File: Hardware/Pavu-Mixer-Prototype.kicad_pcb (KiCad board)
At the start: 2 copper layers, 155.9 x 91.9 mm, 11 parts, among them SW1 SW_MEC_5G_2LED, SW2 SW_MEC_5G_2LED, SW3 SW_MEC_5G_2LED, SW4 SW_MEC_5G_2LED, SW5 SW_MEC_5G_2LED

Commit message: Mounting Holes
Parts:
- added H1: MountingHole_Pad, MountingHole:MountingHole_3.5mm_Pad_Via, F.Cu at (30.4, 29.9)
- added H2: MountingHole_Pad, MountingHole:MountingHole_3.5mm_Pad_Via, F.Cu at (30.4, 112.0)
- added H3: MountingHole_Pad, MountingHole:MountingHole_3.5mm_Pad_Via, F.Cu at (175.4, 29.9)
- added H4: MountingHole_Pad, MountingHole:MountingHole_3.5mm_Pad_Via, F.Cu at (175.4, 112.0)
- moved D1 2.50 mm to (143.8, 42.5)
- moved SW1 2.50 mm to (77.5, 86.7)
- moved SW2 2.50 mm to (77.5, 105.0)
- moved SW3 2.50 mm to (92.5, 86.7)
- moved SW4 2.50 mm to (92.5, 105.0)
- moved SW5 2.50 mm to (147.5, 102.5)
- moved VOL_CH1 2.50 mm to (37.5, 42.5)
- moved VOL_CH2 2.50 mm to (52.5, 42.5)
- moved VOL_CH3 2.50 mm to (110.0, 42.5)
- moved VOL_CH4 2.50 mm to (125.0, 42.5)
- moved VOL_MASTER1 2.50 mm to (162.5, 42.5)

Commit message: GND Net for mounting holes
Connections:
- H1 pad 1: Net-(H1-Pad1) -> GND
- H2 pad 1: Net-(H2-Pad1) -> GND
- H3 pad 1: Net-(H3-Pad1) -> GND
- H4 pad 1: Net-(H4-Pad1) -> GND
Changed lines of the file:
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@@
     (zones 0)
     (modules 15)
-    (nets 5)
+    (nets 2)
   )
   (page A4)
@@
   )
   (net 0 "")
-  (net 1 "Net-(H1-Pad1)")
-  (net 2 "Net-(H2-Pad1)")
-  (net 3 "Net-(H3-Pad1)")
-  (net 4 "Net-(H4-Pad1)")
+  (net 1 GND)
   (net_class Default "This is the default net class."
     (clearance 0.2)
@@
     (uvia_dia 0.3)
     (uvia_drill 0.1)
+    (add_net GND)
     (add_net "Net-(D1-Pad1)")
     (add_net "Net-(D1-Pad10)")
@@
     (add_net "Net-(D1-Pad8)")
     (add_net "Net-(D1-Pad9)")
-    (add_net "Net-(H1-Pad1)")
-    (add_net "Net-(H2-Pad1)")
-    (add_net "Net-(H3-Pad1)")
-    (add_net "Net-(H4-Pad1)")
     (add_net "Net-(SW1-Pad1)")
     (add_net "Net-(SW1-Pad2)")
@@
     (fp_circle (center 0 0) (end 3.75 0) (layer F.CrtYd) (width 0.05))
     (pad 1 thru_hole circle (at 1.856155 -1.856155) (size 0.8 0.8) (drill 0.5) (layers *.Cu *.Mask)
-      (net 4 "Net-(H4-Pad1)"))
+      (net 1 GND))
     (pad 1 thru_hole circle (at 0 -2.625) (size 0.8 0.8) (drill 0.5) (layers *.Cu *.Mask)
-      (net 4 "Net-(H4-Pad1)"))
+      (net 1 GND))
     (pad 1 thru_hole circle (at -1.856155 -1.856155) (size 0.8 0.8) (drill 0.5) (layers *.Cu *.Mask)
-      (net 4 "Net-(H4-Pad1)"))
+      (net 1 GND))
     (pad 1 thru_hole circle (at -2.625 0) (size 0.8 0.8) (drill 0.5) (layers *.Cu *.Mask)
-      (net 4 "Net-(H4-Pad1)"))
+      (net 1 GND))
     (pad 1 thru_hole circle (at -1.856155 1.856155) (size 0.8 0.8) (drill 0.5) (layers *.Cu *.Mask)
-      (net 4 "Net-(H4-Pad1)"))
+      (net 1 GND))
     (pad 1 thru_hole circle (at 0 2.625) (size 0.8 0.8) (drill 0.5) (layers *.Cu *.Mask)
-      (net 4 "Net-(H4-Pad1)"))
+      (net 1 GND))
     (pad 1 thru_hole circle (at 1.856155 1.856155) (size 0.8 0.8) (drill 0.5) (layers *.Cu *.Mask)
-      (net 4 "Net-(H4-Pad1)"))
+      (net 1 GND))
     (pad 1 thru_hole circle (at 2.625 0) (size 0.8 0.8) (drill 0.5) (layers *.Cu *.Mask)
-      (net 4 "Net-(H4-Pad1)"))
+      (net 1 GND))
     (pad 1 thru_hole circle (at 0 0) (size 7 7) (drill 3.5) (layers *.Cu *.Mask)
-      (net 4 "Net-(H4-Pad1)"))
+      (net 1 GND))
   )
   (module MountingHole:MountingHole_3.5mm_Pad_Via (layer F.Cu)
@@
     (fp_circle (center 0 0) (end 3.75 0) (layer F.CrtYd) (width 0.05))
     (pad 1 thru_hole circle (at 1.856155 -1.856155) (size 0.8 0.8) (drill 0.5) (layers *.Cu *.Mask)
-      (net 3 "Net-(H3-Pad1)"))
+      (net 1 GND))
     (pad 1 thru_hole circle (at 0 -2.625) (size 0.8 0.8) (drill 0.5) (layers *.Cu *.Mask)
-      (net 3 "Net-(H3-Pad1)"))
+      (net 1 GND))
     (pad 1 thru_hole circle (at -1.856155 -1.856155) (size 0.8 0.8) (drill 0.5) (layers *.Cu *.Mask)
-      (net 3 "Net-(H3-Pad1)"))
+      (net 1 GND))
     (pad 1 thru_hole circle (at -2.625 0) (size 0.8 0.8) (drill 0.5) (layers *.Cu *.Mask)
-      (net 3 "Net-(H3-Pad1)"))
+      (net 1 GND))
     (pad 1 thru_hole circle (at -1.856155 1.856155) (size 0.8 0.8) (drill 0.5) (layers *.Cu *.Mask)
-      (net 3 "Net-(H3-Pad1)"))
+      (net 1 GND))
     (pad 1 thru_hole circle (at 0 2.625) (size 0.8 0.8) (drill 0.5) (layers *.Cu *.Mask)
-      (net 3 "Net-(H3-Pad1)"))
+      (net 1 GND))
     (pad 1 thru_hole circle (at 1.856155 1.856155) (size 0.8 0.8) (drill 0.5) (layers *.Cu *.Mask)
-      (net 3 "Net-(H3-Pad1)"))
+      (net 1 GND))
     (pad 1 thru_hole circle (at 2.625 0) (size 0.8 0.8) (drill 0.5) (layers *.Cu *.Mask)
-      (net 3 "Net-(H3-Pad1)"))
+      (net 1 GND))
     (pad 1 thru_hole circle (at 0 0) (size 7 7) (drill 3.5) (layers *.Cu *.Mask)
-      (net 3 "Net-(H3-Pad1)"))
+      (net 1 GND))
   )
   (module MountingHole:MountingHole_3.5mm_Pad_Via (layer F.Cu)
@@
     (fp_circle (center 0 0) (end 3.75 0) (layer F.CrtYd) (width 0.05))
     (pad 1 thru_hole circle (at 1.856155 -1.856155) (size 0.8 0.8) (drill 0.5) (layers *.Cu *.Mask)
-      (net 2 "Net-(H2-Pad1)"))
+      (net 1 GND))
     (pad 1 thru_hole circle (at 0 -2.625) (size 0.8 0.8) (drill 0.5) (layers *.Cu *.Mask)
-      (net 2 "Net-(H2-Pad1)"))
+      (net 1 GND))
     (pad 1 thru_hole circle (at -1.856155 -1.856155) (size 0.8 0.8) (drill 0.5) (layers *.Cu *.Mask)
-      (net 2 "Net-(H2-Pad1)"))
+      (net 1 GND))
     (pad 1 thru_hole circle (at -2.625 0) (size 0.8 0.8) (drill 0.5) (layers *.Cu *.Mask)
-      (net 2 "Net-(H2-Pad1)"))
+      (net 1 GND))
     (pad 1 thru_hole circle (at -1.856155 1.856155) (size 0.8 0.8) (drill 0.5) (layers *.Cu *.Mask)
-      (net 2 "Net-(H2-Pad1)"))
+      (net 1 GND))
     (pad 1 thru_hole circle (at 0 2.625) (size 0.8 0.8) (drill 0.5) (layers *.Cu *.Mask)
-      (net 2 "Net-(H2-Pad1)"))
+      (net 1 GND))
     (pad 1 thru_hole circle (at 1.856155 1.856155) (size 0.8 0.8) (drill 0.5) (layers *.Cu *.Mask)
-      (net 2 "Net-(H2-Pad1)"))
+      (net 1 GND))
     (pad 1 thru_hole circle (at 2.625 0) (size 0.8 0.8) (drill 0.5) (layers *.Cu *.Mask)
-      (net 2 "Net-(H2-Pad1)"))
+      (net 1 GND))
     (pad 1 thru_hole circle (at 0 0) (size 7 7) (drill 3.5) (layers *.Cu *.Mask)
-      (net 2 "Net-(H2-Pad1)"))
+      (net 1 GND))
   )
   (module MountingHole:MountingHole_3.5mm_Pad_Via (layer F.Cu)
@@
     (fp_circle (center 0 0) (end 3.75 0) (layer F.CrtYd) (width 0.05))
     (pad 1 thru_hole circle (at 1.856155 -1.856155) (size 0.8 0.8) (drill 0.5) (layers *.Cu *.Mask)
-      (net 1 "Net-(H1-Pad1)"))
+      (net 1 GND))
     (pad 1 thru_hole circle (at 0 -2.625) (size 0.8 0.8) (drill 0.5) (layers *.Cu *.Mask)
-      (net 1 "Net-(H1-Pad1)"))
+      (net 1 GND))
     (pad 1 thru_hole circle (at -1.856155 -1.856155) (size 0.8 0.8) (drill 0.5) (layers *.Cu *.Mask)
-      (net 1 "Net-(H1-Pad1)"))
+      (net 1 GND))
     (pad 1 thru_hole circle (at -2.625 0) (size 0.8 0.8) (drill 0.5) (layers *.Cu *.Mask)
-      (net 1 "Net-(H1-Pad1)"))
+      (net 1 GND))
     (pad 1 thru_hole circle (at -1.856155 1.856155) (size 0.8 0.8) (drill 0.5) (layers *.Cu *.Mask)
-      (net 1 "Net-(H1-Pad1)"))
+      (net 1 GND))
     (pad 1 thru_hole circle (at 0 2.625) (size 0.8 0.8) (drill 0.5) (layers *.Cu *.Mask)
-      (net 1 "Net-(H1-Pad1)"))
+      (net 1 GND))
     (pad 1 thru_hole circle (at 1.856155 1.856155) (size 0.8 0.8) (drill 0.5) (layers *.Cu *.Mask)
-      (net 1 "Net-(H1-Pad1)"))
+      (net 1 GND))
     (pad 1 thru_hole circle (at 2.625 0) (size 0.8 0.8) (drill 0.5) (layers *.Cu *.Mask)
-      (net 1 "Net-(H1-Pad1)"))
+      (net 1 GND))
     (pad 1 thru_hole circle (at 0 0) (size 7 7) (drill 3.5) (layers *.Cu *.Mask)
-      (net 1 "Net-(H1-Pad1)"))
+      (net 1 GND))
   )
   (module Pavu-Mixer-Prototype:Potentiometer_Alps_RS60_Double_Slide (layer F.Cu)

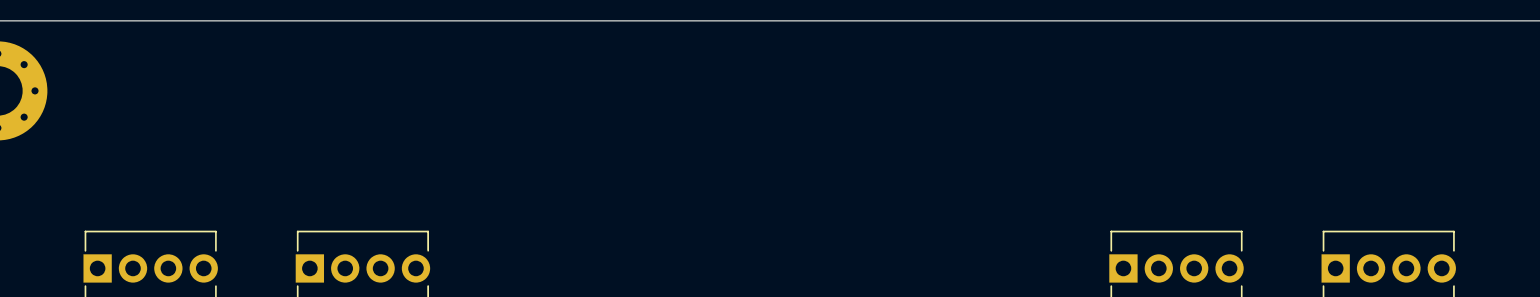
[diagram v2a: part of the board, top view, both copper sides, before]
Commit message: Add channel LEDs
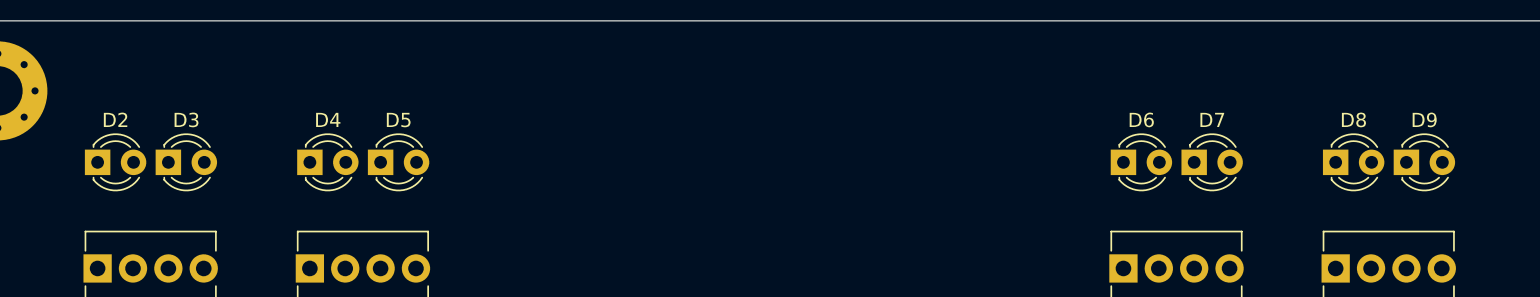
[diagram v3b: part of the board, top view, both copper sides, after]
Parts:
- added D2: LED, LED_THT:LED_D3.0mm, F.Cu at (37.5, 35.0)
- added D3: LED, LED_THT:LED_D3.0mm_Clear, F.Cu at (42.5, 35.0)
- added D4: LED, LED_THT:LED_D3.0mm, F.Cu at (52.5, 35.0)
- added D5: LED, LED_THT:LED_D3.0mm_Clear, F.Cu at (57.5, 35.0)
- added D6: LED, LED_THT:LED_D3.0mm, F.Cu at (110.0, 35.0)
- added D7: LED, LED_THT:LED_D3.0mm_Clear, F.Cu at (115.0, 35.0)
- added D8: LED, LED_THT:LED_D3.0mm, F.Cu at (125.0, 35.0)
- added D9: LED, LED_THT:LED_D3.0mm_Clear, F.Cu at (130.0, 35.0)

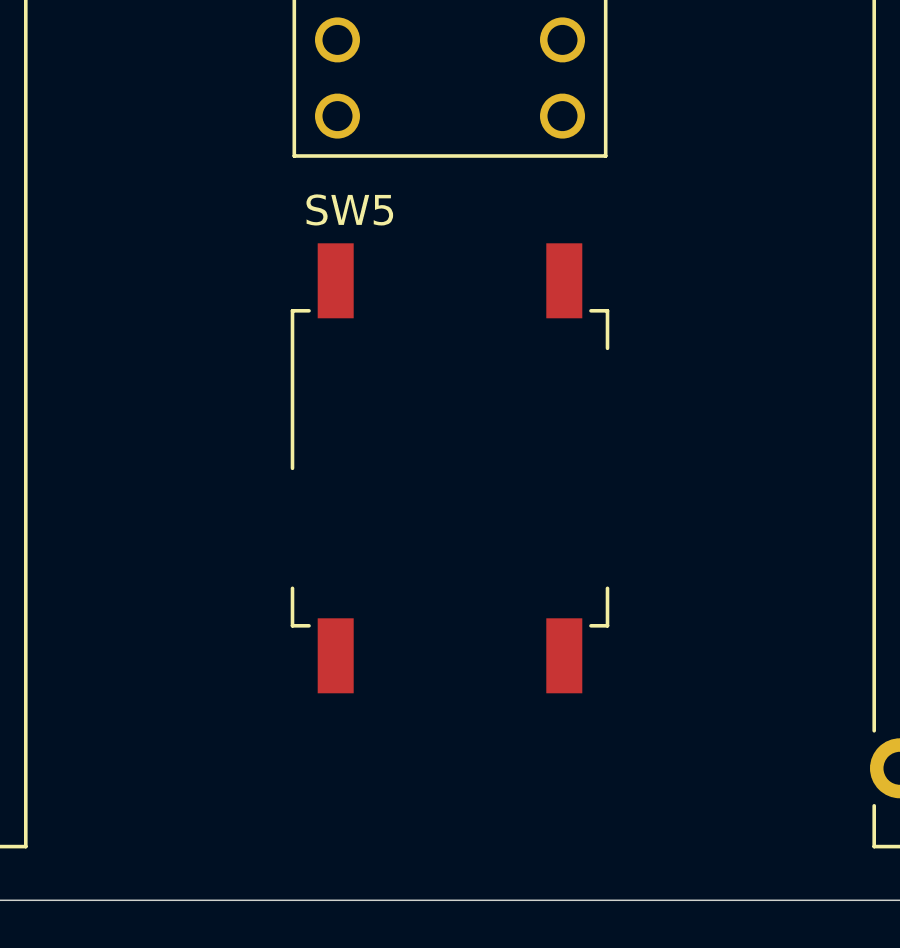
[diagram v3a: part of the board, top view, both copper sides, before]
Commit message: Fix master mute position
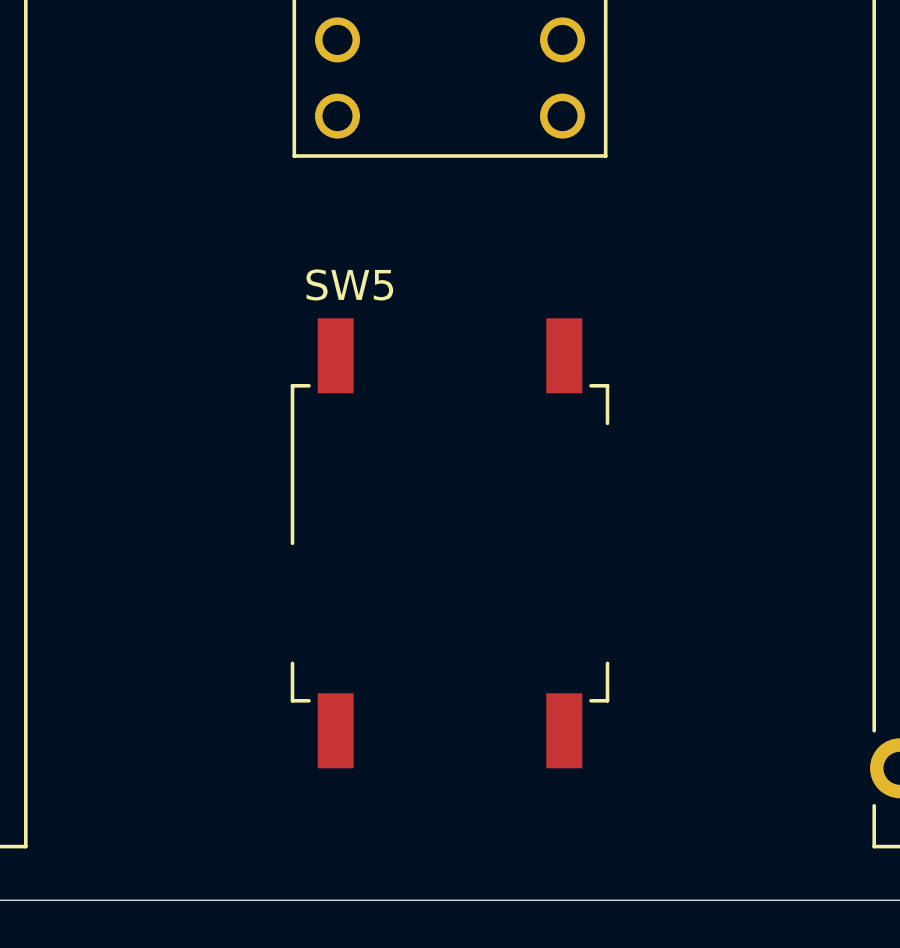
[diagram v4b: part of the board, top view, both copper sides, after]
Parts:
- moved SW5 2.50 mm to (147.5, 105.0)
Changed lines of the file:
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@@
   )
   (module Pavu-Mixer-Prototype:SW_MEC_5GSH9 (layer F.Cu)
-    (at 147.5 102.5)
+    (at 147.5 105)
     (descr "MEC 5G single pole normally-open tactile switch")
     (tags "switch normally-open pushbutton push-button")

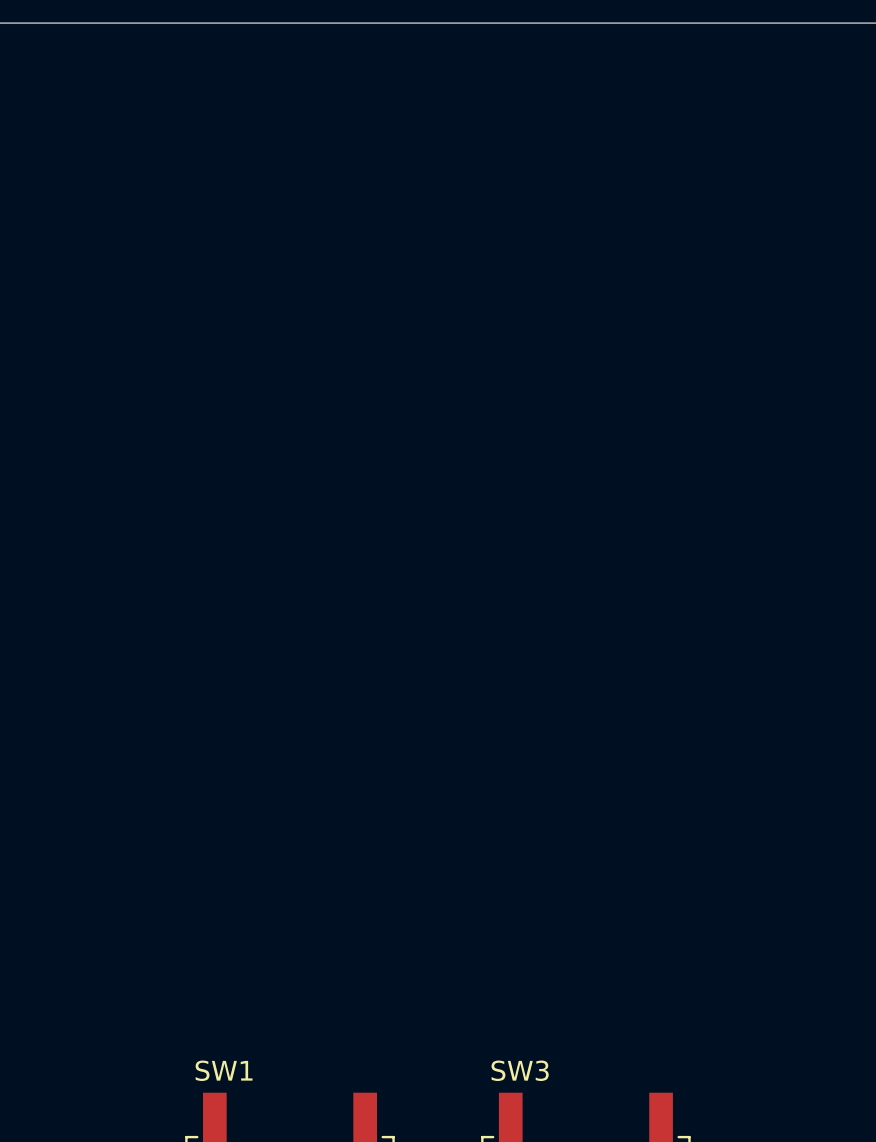
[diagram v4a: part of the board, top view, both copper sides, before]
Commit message: Add display to PCB sketch
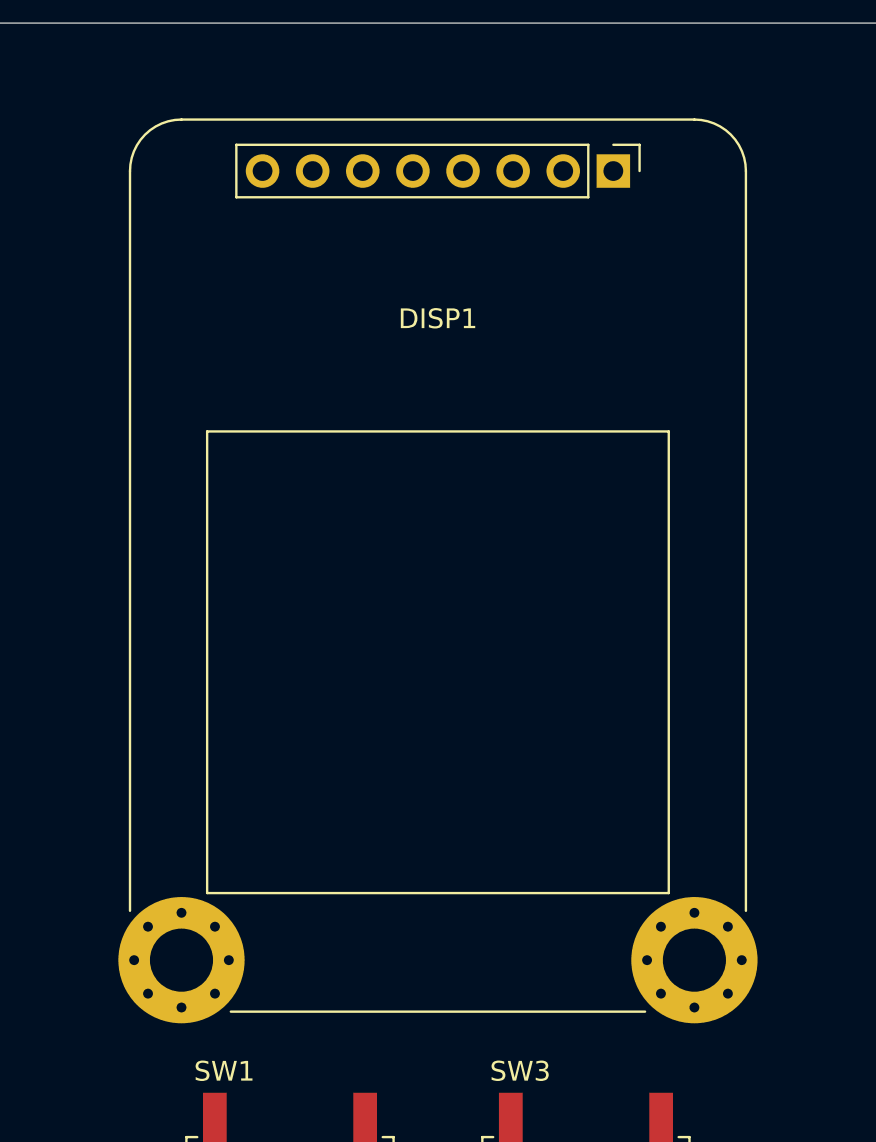
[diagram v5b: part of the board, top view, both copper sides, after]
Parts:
- added DISP1: Waveshare_LCD_240X240, Pavu-Mixer-Prototype:Waveshare_LCD_240X240, F.Cu at (85.0, 32.5)
